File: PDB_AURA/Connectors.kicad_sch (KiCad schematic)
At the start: 29 parts, among them J300 XT30PW-F, J301 XT30PW-F, J302 532617012, J303 XT30PW-F, J304 XT30PW-F, Q300 HSK10N06, Q301 HSK10N06, U300 LTV-217-B-G, U301 LTV-217-B-G, U302 INA219AIDCNR

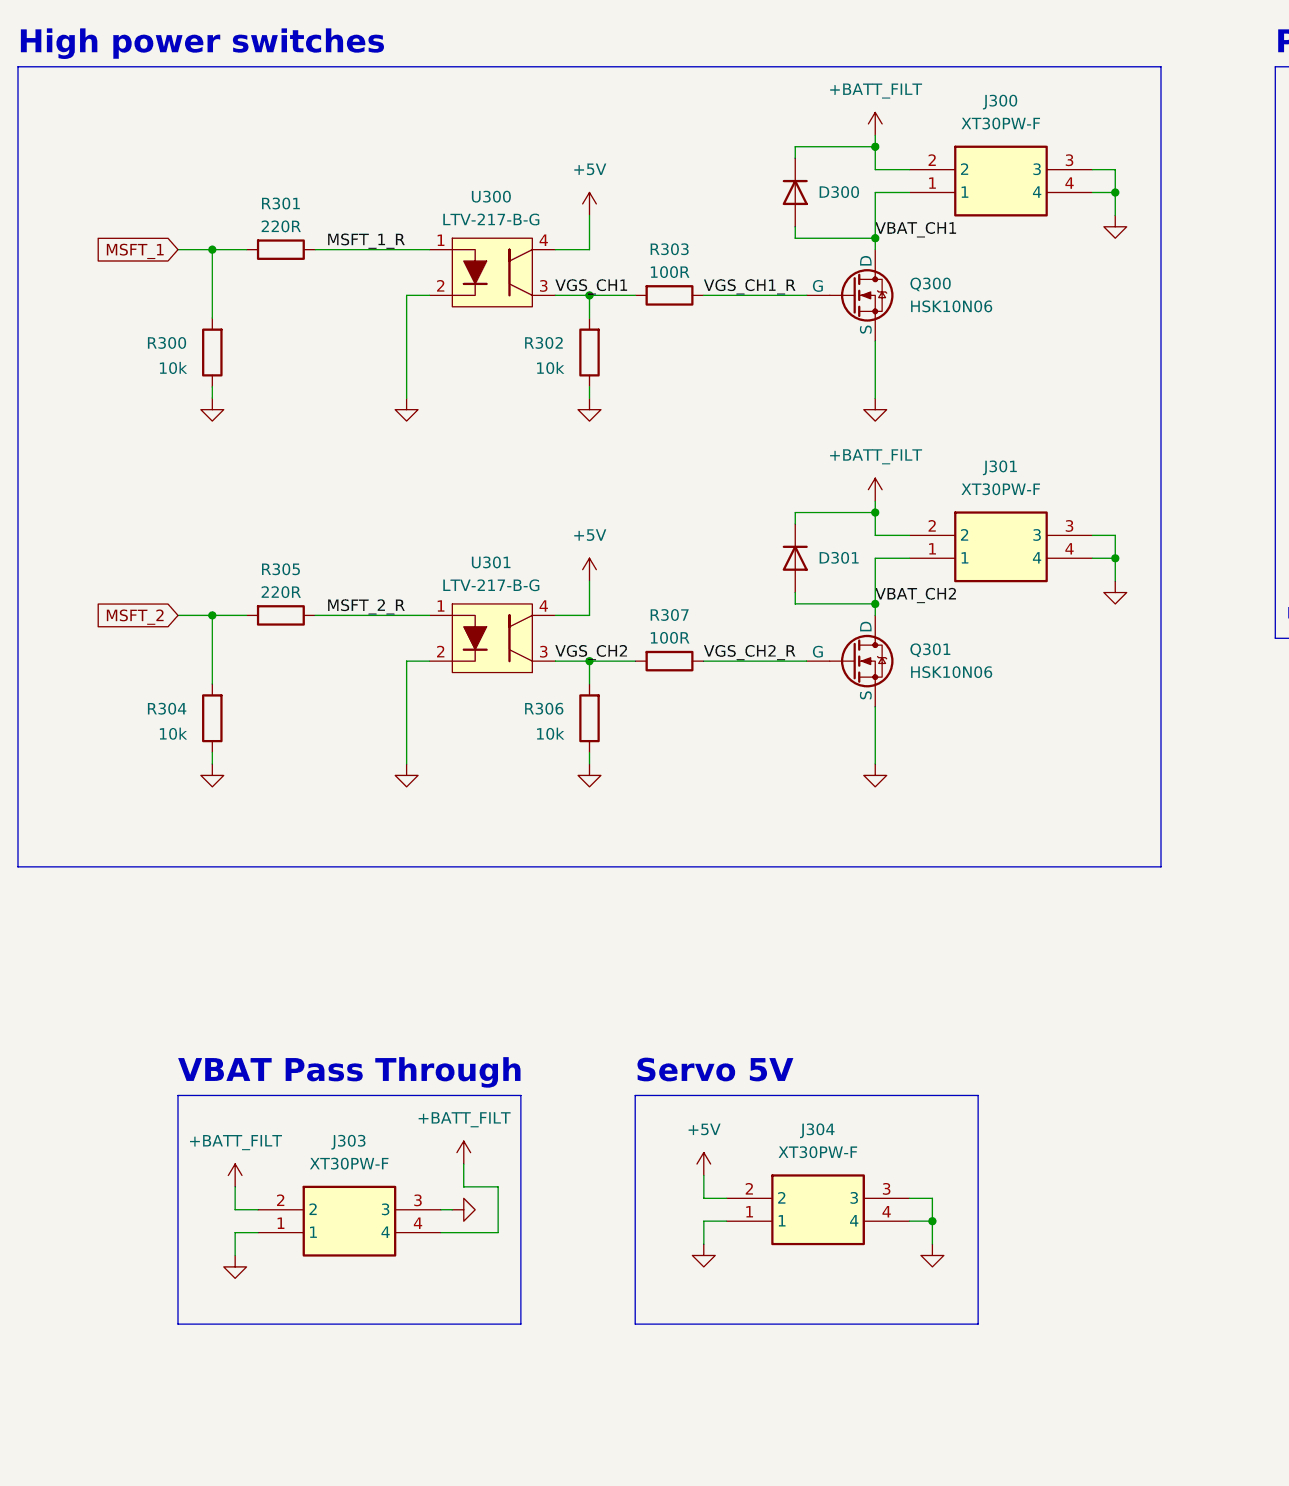
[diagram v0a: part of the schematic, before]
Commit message: Silk Screen Done
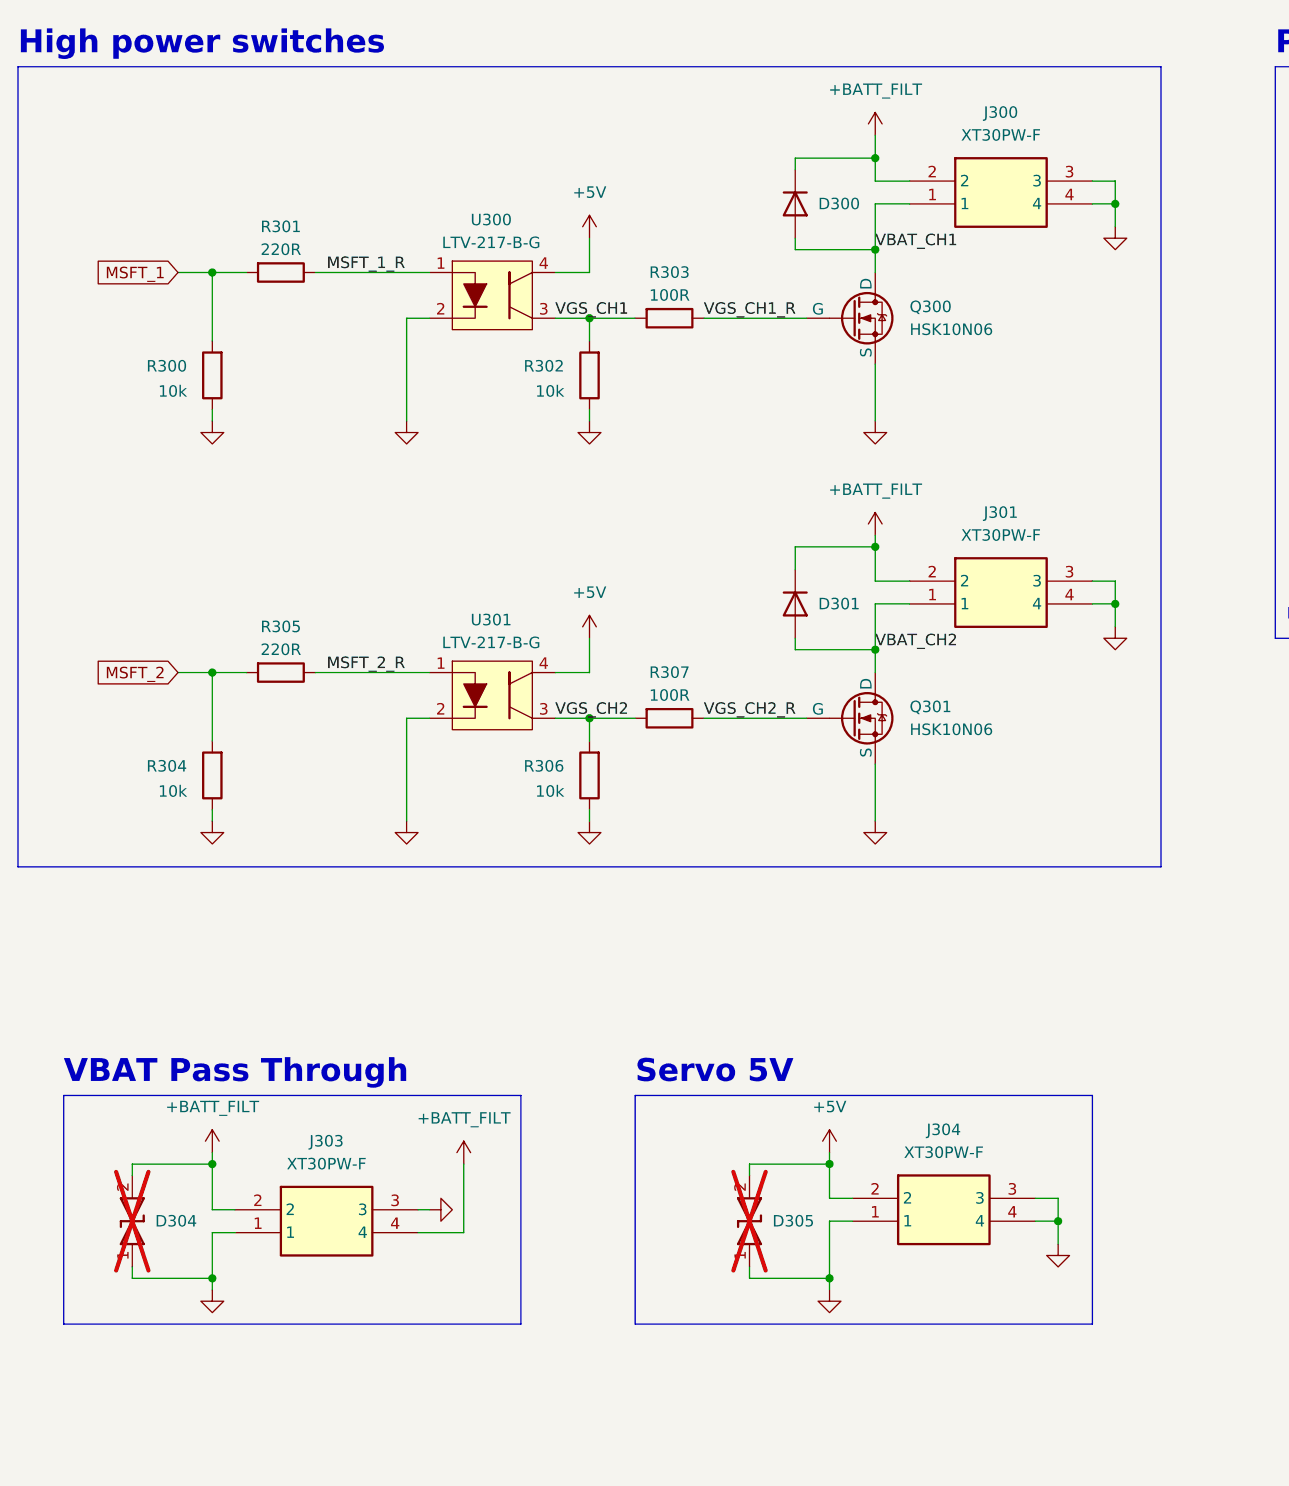
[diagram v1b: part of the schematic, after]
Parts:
- added D304, D305: SMBJ33CA, DIONM5436X244N, symbol SMBJ33CA:SMBJ33CA
- J302: now left out of the parts list
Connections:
- net +5V: now also D305.2
- net +BATT_FILT: now also D304.2
- net GND: now also D304.1, D305.1
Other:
- moved on the sheet: D300, D301, J300, J301, J303, J304, Q300, Q301, R300, R301, R302, R303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

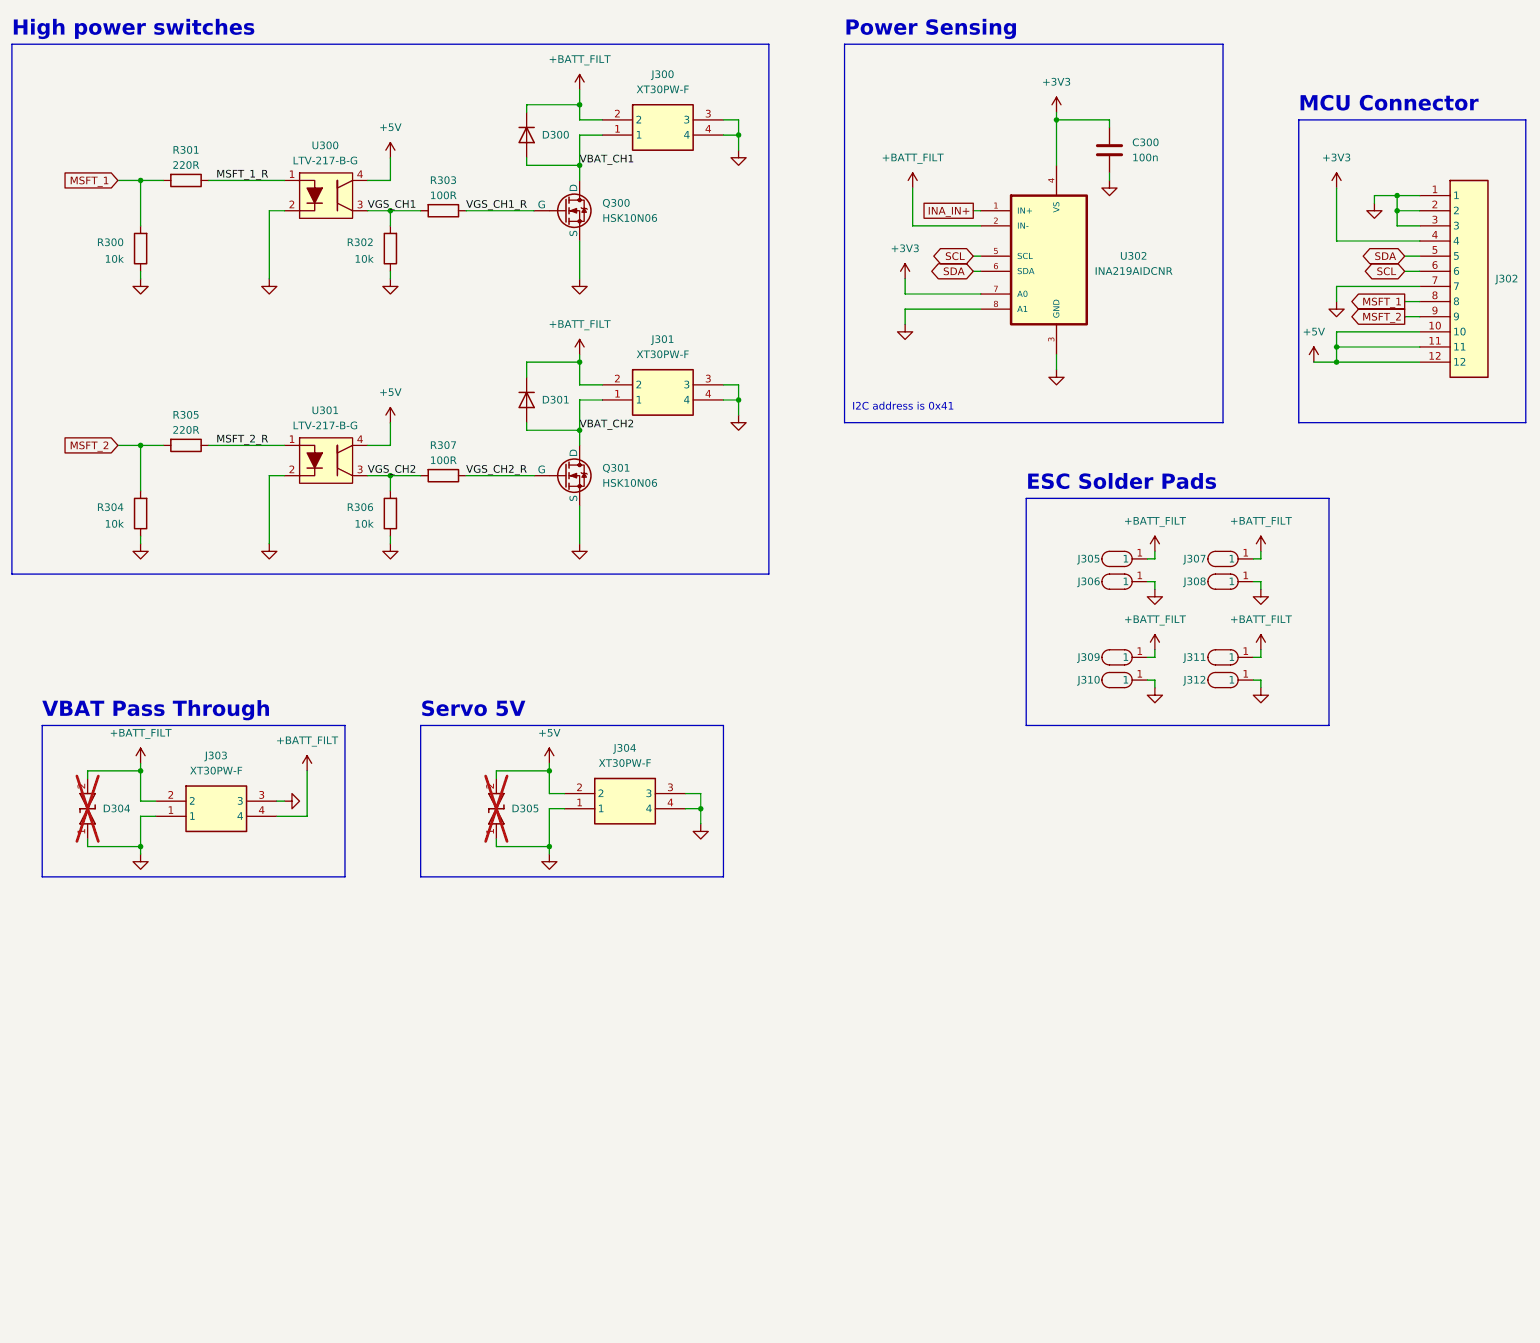
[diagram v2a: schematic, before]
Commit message: Tidied up PDB schematic for documentation.
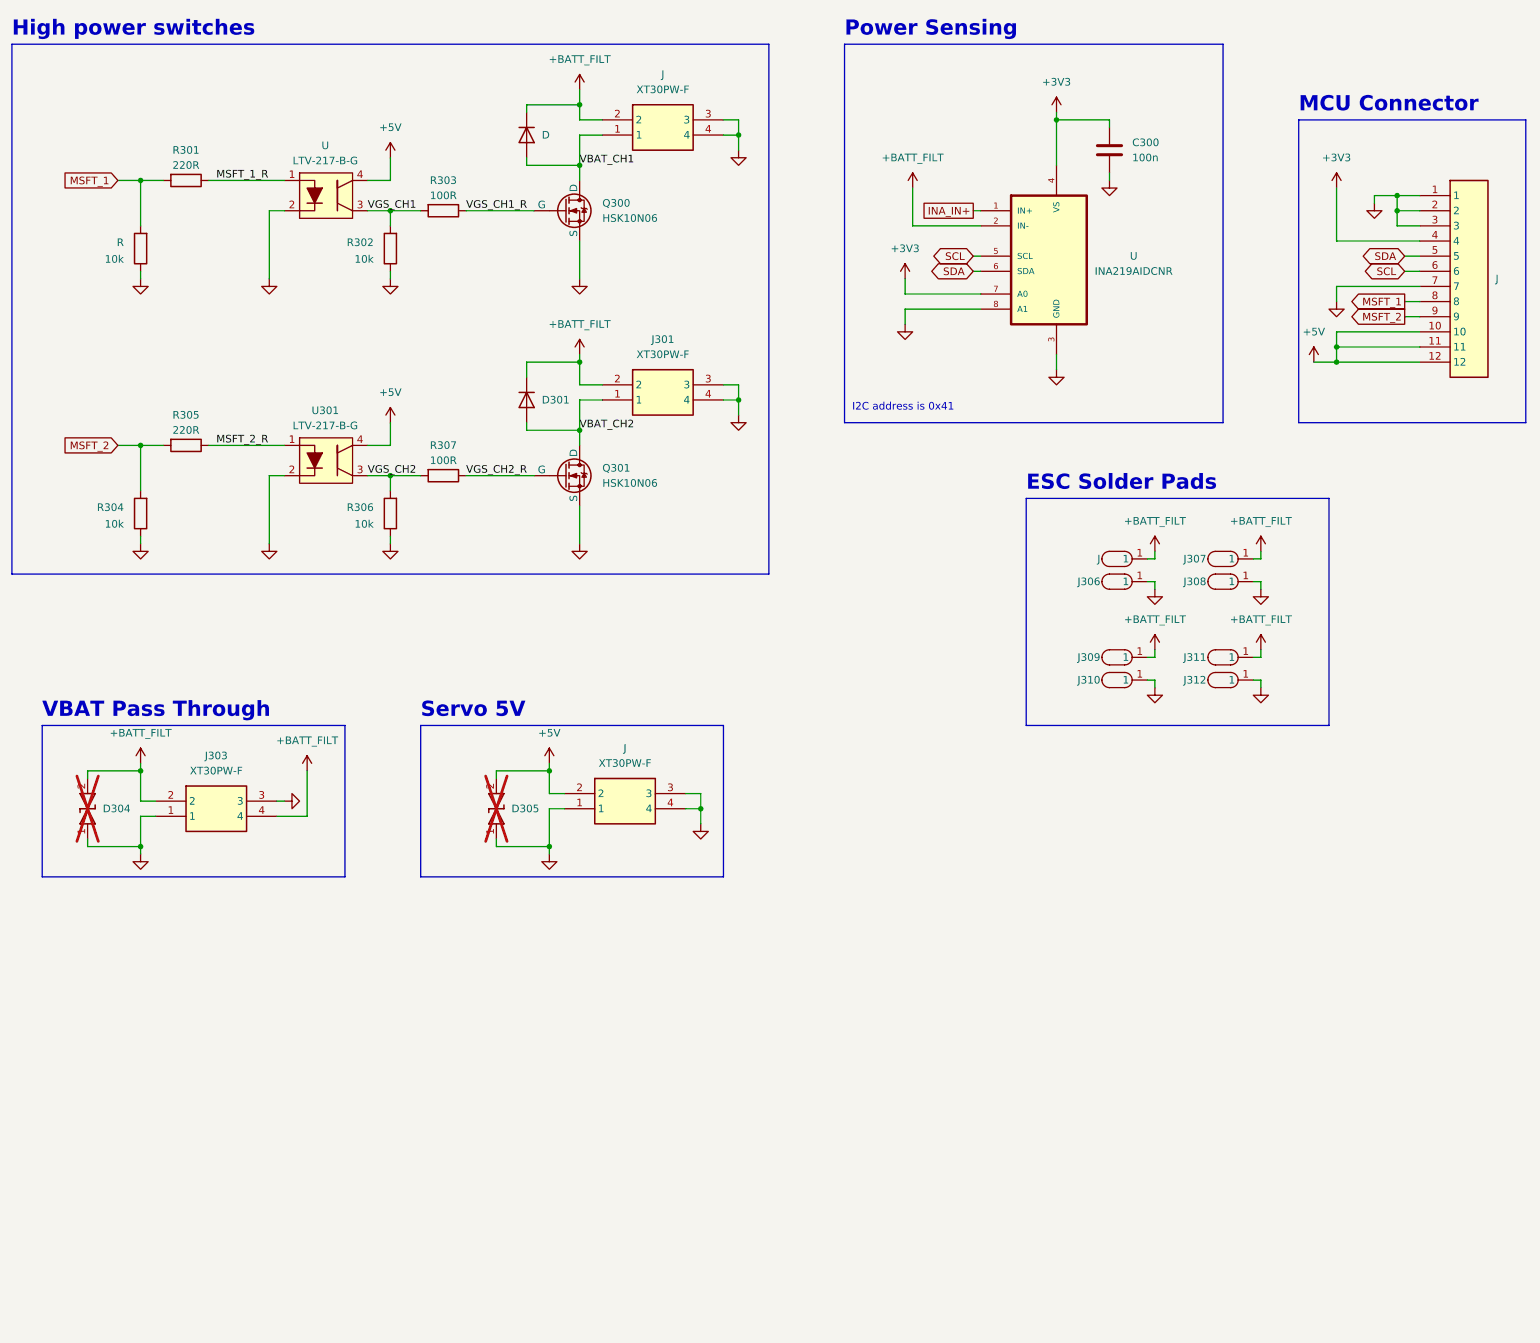
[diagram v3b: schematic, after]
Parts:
- renumbered D300 to D, J300 to J, J305 to J, J304 to J, J302 to J, R300 to R, U302 to U, U300 to U
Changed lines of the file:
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@@
 		(on_board yes)
 		(dnp no)
-		(property "Reference" "R300"
+		(property "Reference" "R"
 			(at 39.116 71.374 0)
 			(effects
@@
 		(pin "2"
 		)
-		(instances
-			(project "Summer2025"
-				(path "/c0b09de1-c640-438f-9ef5-dda14a6aac71/bf94e7c9-9821-4c41-aadb-9bb6d92f20f0"
-					(reference "R300")
-					(unit 1)
-				)
-			)
-		)
+		(instances)
 	)
 	(symbol
@@
 		(dnp no)
 		(fields_autoplaced yes)
-		(property "Reference" "#PWR027"
+		(property "Reference" "#PWR"
 			(at 110.49 180.34 0)
 			(effects
@@
 		(pin "1"
 		)
-		(instances
-			(project "MCU_AURA"
-				(path "/c0b09de1-c640-438f-9ef5-dda14a6aac71/bf94e7c9-9821-4c41-aadb-9bb6d92f20f0"
-					(reference "#PWR027")
-					(unit 1)
-				)
-			)
-		)
+		(instances)
 	)
 	(symbol
@@
 		(dnp no)
 		(fields_autoplaced yes)
-		(property "Reference" "#PWR06"
+		(property "Reference" "#PWR"
 			(at 41.91 83.82 0)
 			(effects
@@
 		(pin "1"
 		)
-		(instances
-			(project "Summer2025"
-				(path "/c0b09de1-c640-438f-9ef5-dda14a6aac71/bf94e7c9-9821-4c41-aadb-9bb6d92f20f0"
-					(reference "#PWR06")
-					(unit 1)
-				)
-			)
-		)
+		(instances)
 	)
 	(symbol
@@
 		(on_board yes)
 		(dnp no)
-		(property "Reference" "U302"
+		(property "Reference" "U"
 			(at 208.534 73.66 0)
 			(effects
@@
 		(pin "1"
 		)
-		(instances
-			(project ""
-				(path "/c0b09de1-c640-438f-9ef5-dda14a6aac71/bf94e7c9-9821-4c41-aadb-9bb6d92f20f0"
-					(reference "U302")
-					(unit 1)
-				)
-			)
-		)
+		(instances)
 	)
 	(symbol
@@
 		(dnp no)
 		(fields_autoplaced yes)
-		(property "Reference" "#PWR033"
+		(property "Reference" "#PWR"
 			(at 115.57 49.53 0)
 			(effects
@@
 		(pin "1"
 		)
-		(instances
-			(project "MCU_AURA"
-				(path "/c0b09de1-c640-438f-9ef5-dda14a6aac71/bf94e7c9-9821-4c41-aadb-9bb6d92f20f0"
-					(reference "#PWR033")
-					(unit 1)
-				)
-			)
-		)
+		(instances)
 	)
 	(symbol
@@
 		(dnp no)
 		(fields_autoplaced yes)
-		(property "Reference" "#PWR031"
+		(property "Reference" "#PWR"
 			(at 142.24 62.23 0)
 			(effects
@@
 		(pin "1"
 		)
-		(instances
-			(project "MCU_AURA"
-				(path "/c0b09de1-c640-438f-9ef5-dda14a6aac71/bf94e7c9-9821-4c41-aadb-9bb6d92f20f0"
-					(reference "#PWR031")
-					(unit 1)
-				)
-			)
-		)
+		(instances)
 	)
 	(symbol
@@
 		(dnp no)
 		(fields_autoplaced yes)
-		(property "Reference" "J300"
+		(property "Reference" "J"
 			(at 129.54 43.18 0)
 			(effects
@@
 		(pin "1"
 		)
-		(instances
-			(project ""
-				(path "/c0b09de1-c640-438f-9ef5-dda14a6aac71/bf94e7c9-9821-4c41-aadb-9bb6d92f20f0"
-					(reference "J300")
-					(unit 1)
-				)
-			)
-		)
+		(instances)
 	)
 	(symbol
@@
 		(dnp no)
 		(fields_autoplaced yes)
-		(property "Reference" "#PWR035"
+		(property "Reference" "#PWR"
 			(at 110.49 162.56 0)
 			(effects
@@
 		(pin "1"
 		)
-		(instances
-			(project "MCU_AURA"
-				(path "/c0b09de1-c640-438f-9ef5-dda14a6aac71/bf94e7c9-9821-4c41-aadb-9bb6d92f20f0"
-					(reference "#PWR035")
-					(unit 1)
-				)
-			)
-		)
+		(instances)
 	)
 	(symbol
@@
 		(on_board yes)
 		(dnp no)
-		(property "Reference" "U300"
+		(property "Reference" "U"
 			(at 72.898 55.118 0)
 			(effects
@@
 		(pin "3"
 		)
-		(instances
-			(project ""
-				(path "/c0b09de1-c640-438f-9ef5-dda14a6aac71/bf94e7c9-9821-4c41-aadb-9bb6d92f20f0"
-					(reference "U300")
-					(unit 1)
-				)
-			)
-		)
+		(instances)
 	)
 	(symbol
@@
 		(on_board yes)
 		(dnp no)
-		(property "Reference" "J305"
+		(property "Reference" "J"
 			(at 202.946 124.46 0)
 			(effects
@@
 		(pin "1"
 		)
-		(instances
-			(project ""
-				(path "/c0b09de1-c640-438f-9ef5-dda14a6aac71/bf94e7c9-9821-4c41-aadb-9bb6d92f20f0"
-					(reference "J305")
-					(unit 1)
-				)
-			)
-		)
+		(instances)
 	)
 	(symbol
@@
 		(dnp no)
 		(fields_autoplaced yes)
-		(property "Reference" "J304"
+		(property "Reference" "J"
 			(at 123.19 156.21 0)
 			(effects
@@
 		(pin "1"
 		)
-		(instances
-			(project "MCU_AURA"
-				(path "/c0b09de1-c640-438f-9ef5-dda14a6aac71/bf94e7c9-9821-4c41-aadb-9bb6d92f20f0"
-					(reference "J304")
-					(unit 1)
-				)
-			)
-		)
+		(instances)
 	)
 	(symbol
@@
 		(dnp no)
 		(fields_autoplaced yes)
-		(property "Reference" "J302"
+		(property "Reference" "J"
 			(at 269.24 77.4699 0)
 			(effects
@@
 		(pin "4"
 		)
-		(instances
-			(project ""
-				(path "/c0b09de1-c640-438f-9ef5-dda14a6aac71/bf94e7c9-9821-4c41-aadb-9bb6d92f20f0"
-					(reference "J302")
-					(unit 1)
-				)
-			)
-		)
+		(instances)
 	)
 	(symbol
@@
 		(dnp no)
 		(fields_autoplaced yes)
-		(property "Reference" "#PWR030"
+		(property "Reference" "#PWR"
 			(at 135.89 175.26 0)
 			(effects
@@
 		(pin "1"
 		)
-		(instances
-			(project "MCU_AURA"
-				(path "/c0b09de1-c640-438f-9ef5-dda14a6aac71/bf94e7c9-9821-4c41-aadb-9bb6d92f20f0"
-					(reference "#PWR030")
-					(unit 1)
-				)
-			)
-		)
+		(instances)
 	)
 	(symbol
@@
 		(dnp no)
 		(fields_autoplaced yes)
-		(property "Reference" "D300"
+		(property "Reference" "D"
 			(at 109.22 53.3399 90)
 			(effects
@@
 		(pin "2"
 		)
-		(instances
-			(project ""
-				(path "/c0b09de1-c640-438f-9ef5-dda14a6aac71/bf94e7c9-9821-4c41-aadb-9bb6d92f20f0"
-					(reference "D300")
-					(unit 1)
-				)
-			)
-		)
+		(instances)
 	)
 	(symbol
